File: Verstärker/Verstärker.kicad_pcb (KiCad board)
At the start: 2 copper layers, 59 parts, among them J3 ACJS-MHOM, J4 NRJ6HM-1, Q1 MJE13005G, Q1 MJE182G, Q12 MMBT5401, Q12 NPN, Q13 MMBT5401, Q13 NPN, Q2 MJE13005G, Q2 MJE172G, Q3 MMBT5551(RANGE:200-300), Q9 MMBT5551(RANGE:200-300)

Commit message: 29.04. Ende der VL
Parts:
- removed the Q1 at (207.0, 64.4)
- removed the Q1 at (237.5, 106.4)
- removed the Q12 at (77.0, 92.1)
- removed the Q12 at (237.5, 115.3)
- removed the Q13 at (52.0, 92.1)
- removed the Q13 at (237.5, 120.0)
- removed the Q2 at (163.0, 127.9)
- removed the Q2 at (237.5, 111.0)
- removed the TP3 at (209.5, 56.5)
- removed the TP3 at (157.8, 14.0)
- removed TP_GND1, TP_R2, TP_T2: OUT, TestPoint:TestPoint_Pad_D1.0mm
- removed TP_R1: IN, TestPoint:TestPoint_Pad_D1.0mm
- removed TP_S1: VCC -, TestPoint:TestPoint_Pad_D1.0mm
- added H1: OUT AMP B, MountingHole:MountingHole_2.2mm_M2_Pad_TopBottom, F.Cu at (167.8, 66.1)
- added H2: IN, MountingHole:MountingHole_2.2mm_M2_Pad_TopBottom, F.Cu at (53.0, 121.0)
- added H3: VCC +, MountingHole:MountingHole_2.2mm_M2_Pad_TopBottom, F.Cu at (167.8, 106.1)
- added H4: VCC -, MountingHole:MountingHole_2.2mm_M2_Pad_TopBottom, F.Cu at (153.8, 106.1)
- added H5: GND, MountingHole:MountingHole_2.2mm_M2_Pad_TopBottom, F.Cu at (37.5, 121.0)
- added H6: VCC GND, MountingHole:MountingHole_2.2mm_M2_Pad_TopBottom, F.Cu at (160.8, 106.1)
- added H7: GND, MountingHole:MountingHole_2.2mm_M2_Pad_TopBottom, F.Cu at (160.3, 66.1)
- added H8: OUT, MountingHole:MountingHole_2.2mm_M2_Pad_TopBottom, F.Cu at (152.8, 66.1)
- added H9: IN AMP B, MountingHole:MountingHole_2.2mm_M2_Pad_TopBottom, F.Cu at (45.5, 121.0)
- added Q1: MJE182G, project-custom:TO229P780X300X1364-3, F.Cu at (144.9, 77.1)
- added Q12: MMBT5401, Package_TO_SOT_SMD:SOT-23, F.Cu at (94.9, 82.5)
- added Q13: MMBT5401, Package_TO_SOT_SMD:SOT-23, F.Cu at (81.0, 82.5)
- added Q2: MJE172G, project-custom:TO229P780X300X1364-3, F.Cu at (144.8, 99.1)
- added TP3: Q2, TestPoint:TestPoint_Pad_D2.0mm, F.Cu at (143.2, 127.4)
- TP1: value TestPoint -> Output
- TP12: value TestPoint -> GND
- TP2: value TestPoint -> Q1
- moved TP12 144.4 mm to (73.0, 121.0)
- moved TP11 142.6 mm to (80.5, 121.0)
- moved TP10 141.0 mm to (88.5, 121.0)
- moved TP7 126.2 mm to (134.0, 128.0)
- moved TP1 120.2 mm to (162.5, 126.0)
- moved TP5 101.7 mm to (72.0, 57.5)
- moved J4 99.1 mm to (160.3, 80.2)
- moved TP8 94.1 mm to (85.0, 58.0)
- moved R12 85.2 mm to (129.8, 88.2), turned to -90 degrees
- moved C2 84.3 mm to (129.8, 83.8), turned to 90 degrees
- moved TP9 83.5 mm to (95.0, 58.0)
- moved TP4 78.3 mm to (103.5, 58.0)
- moved R4 76.1 mm to (136.0, 89.5), turned to 90 degrees
- moved TP6 66.3 mm to (109.0, 54.0)
- moved C1 64.1 mm to (100.0, 92.0), turned to 90 degrees
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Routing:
- net GND: track 0.00 -> 64.4 mm
- net Net-(D9-K): track 0.00 -> 43.6 mm
- net Net-(D1-A): track 0.00 -> 26.7 mm
- net Net-(D10-A): track 0.00 -> 12.9 mm
- net Net-(Q1-E): track 0.00 -> 3.94 mm
- net Net-(Q2-E): track 0.00 -> 3.92 mm

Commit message: 29.04. 15 Uhr
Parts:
- moved R8 19.3 mm to (63.0, 102.8)
- moved R13 16.5 mm to (57.5, 104.2)
- moved C6 15.5 mm to (67.8, 103.5)
- moved C7 15.0 mm to (65.5, 98.0)
- moved C4 14.6 mm to (94.2, 89.2), turned to 180 degrees
- moved TP9 12.6 mm to (82.8, 60.8)
- moved R10 9.60 mm to (87.8, 84.8), turned to 0 degrees
- moved C1 6.75 mm to (99.8, 98.8)
- moved TP8 6.56 mm to (89.2, 63.0)
- moved R7 6.52 mm to (99.5, 92.0)
- moved R3 6.49 mm to (87.8, 79.5), turned to 180 degrees
- moved D2 4.30 mm to (87.8, 88.2), turned to 180 degrees
- moved D3 3.56 mm to (87.8, 94.0), turned to 0 degrees
- moved Q13 2.11 mm to (79.8, 84.2), turned to 90 degrees
- moved R9 0.51 mm to (74.2, 84.5)
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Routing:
- net Net-(D2-K): track 0.00 -> 32.5 mm
- net Net-(Q12-E): track 0.00 -> 23.8 mm, vias 0 -> 2
- net Net-(D2-A): track 0.00 -> 20.0 mm
- net Net-(D10-A): track 12.9 -> 26.8 mm
- net Net-(Q13-C): track 0.00 -> 7.05 mm
- net Net-(C1-Pad2): track 0.00 -> 3.74 mm

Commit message: 04.05. PCB komplett
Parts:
- moved TP1 44.6 mm to (135.8, 90.3)
- moved TP3 36.0 mm to (128.6, 94.5)
- moved TP7 33.9 mm to (115.7, 99.5)
- moved R4 33.6 mm to (105.1, 102.6), turned to 0 degrees
- moved TP11 32.7 mm to (109.7, 106.1)
- moved TP2 26.4 mm to (127.5, 80.3)
- moved R14 24.9 mm to (101.0, 94.6), turned to 0 degrees
- moved TP12 24.6 mm to (90.0, 103.2)
- moved TP10 22.0 mm to (96.9, 100.7)
- moved TP4 22.0 mm to (98.9, 79.5)
- moved TP5 21.8 mm to (74.9, 79.1)
- moved TP6 21.2 mm to (124.5, 68.5)
- moved H1 20.2 mm to (147.7, 66.3)
- moved H2 20.1 mm to (64.2, 104.3)
- moved H5 20.1 mm to (48.7, 104.3)
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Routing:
- net Net-(D10-A): track 26.8 -> 102.2 mm, vias 0 -> 2
- net Net-(D1-A): track 26.7 -> 84.9 mm
- net Net-(D9-K): track 43.6 -> 96.7 mm
- net Net-(D1-K): track 0.00 -> 52.7 mm, vias 0 -> 2
- net Net-(D4-A): track 0.00 -> 46.9 mm, vias 0 -> 2
- net Net-(Q13-C): track 7.05 -> 31.2 mm
- net Net-(H2-Pad1): track 0.00 -> 23.1 mm
- net GND: track 64.4 -> 45.1 mm
- net Net-(H1-Pad1): track 0.00 -> 16.8 mm
- net Net-(D2-A): track 20.0 -> 30.5 mm
- net Net-(H9-Pad1): track 0.00 -> 10.1 mm
- net Net-(C6-Pad2): track 0.00 -> 8.57 mm
- net Net-(Q3-B): track 0.00 -> 7.03 mm
- net Net-(Q1-E): track 3.94 -> 9.29 mm
- net Net-(Q12-E): track 23.8 -> 29.0 mm
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- added copper zone on B.Cu, net GND
- added copper zone on F.Cu, net GND

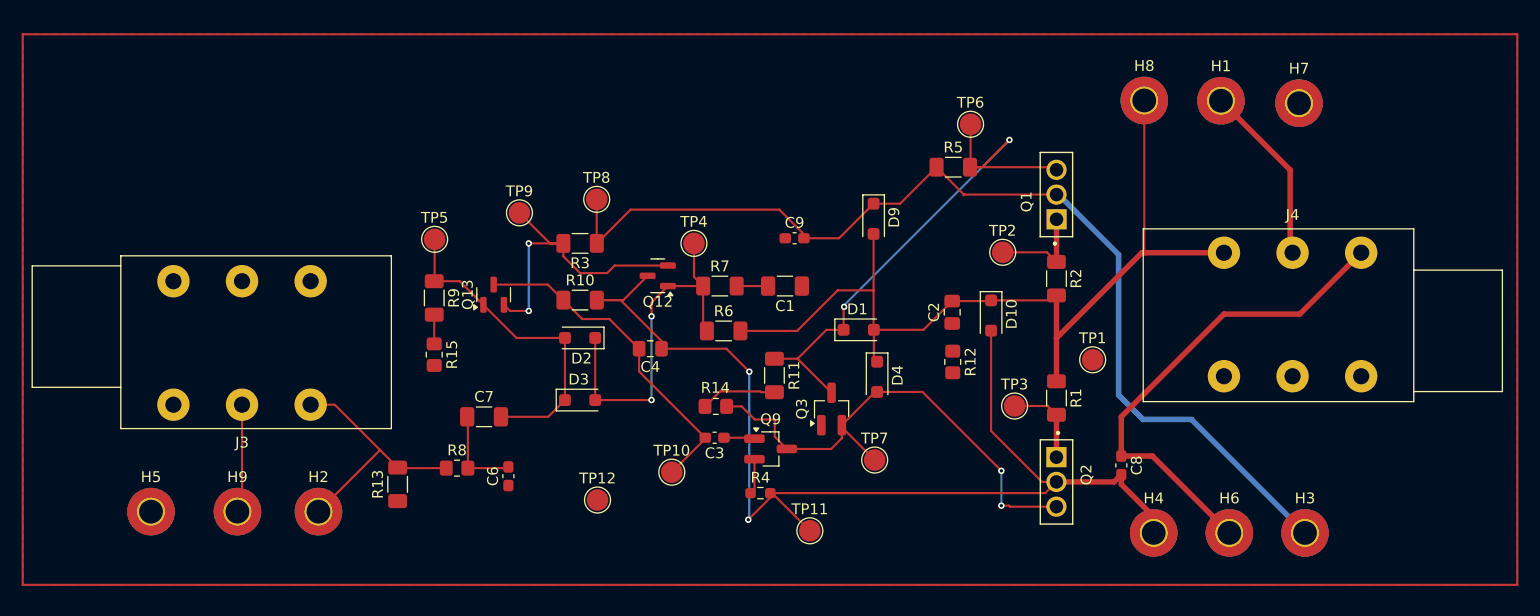
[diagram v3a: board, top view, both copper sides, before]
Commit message: dru Datei hinnzugefügt. Silcscreen der Testpoitns angepasst.
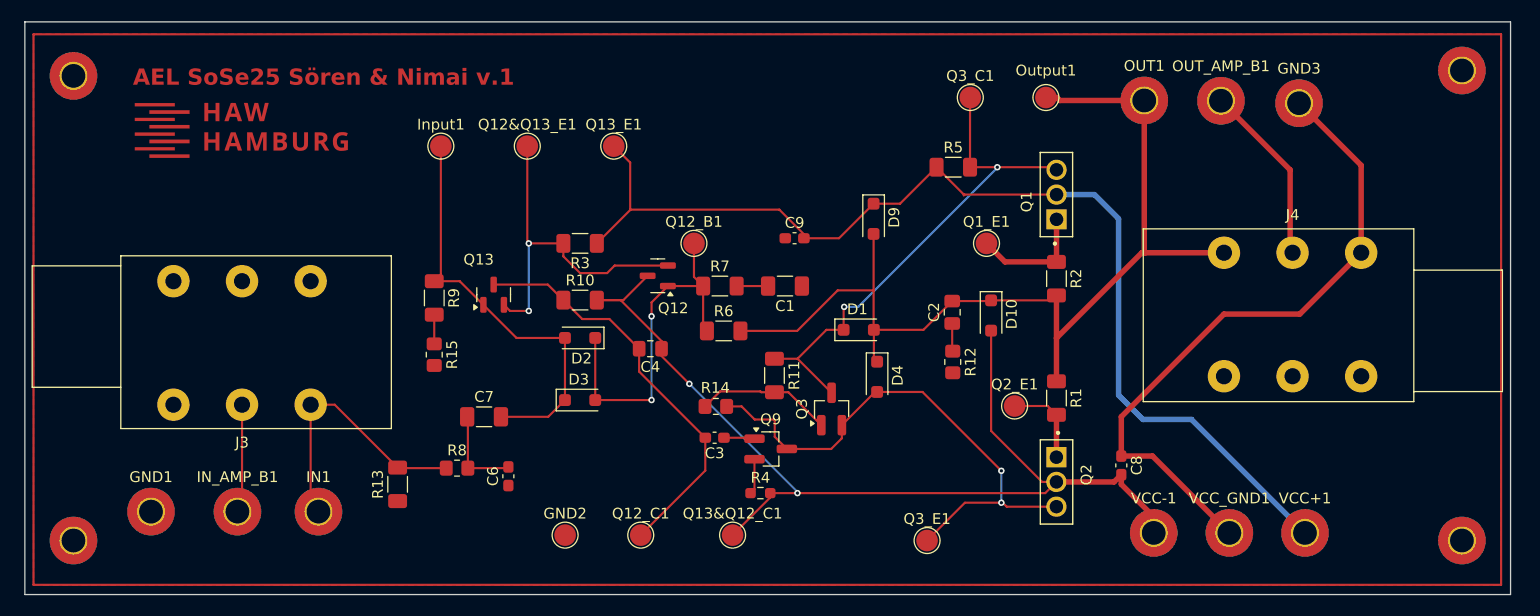
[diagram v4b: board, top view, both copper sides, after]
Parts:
- added G***: LOGO, LOGO, F.Cu at (57.0, 69.0)
- added GND4: H5, MountingHole:MountingHole_2.2mm_M2_Pad_TopBottom, F.Cu at (41.5, 64.0)
- added GND5: H5, MountingHole:MountingHole_2.2mm_M2_Pad_TopBottom, F.Cu at (41.5, 107.0)
- added GND6: H5, MountingHole:MountingHole_2.2mm_M2_Pad_TopBottom, F.Cu at (170.0, 63.5)
- added GND7: H5, MountingHole:MountingHole_2.2mm_M2_Pad_TopBottom, F.Cu at (170.0, 107.0)
- GND1: renamed from H5; value GND -> H5
- GND2: renamed from TP12; value GND -> TP12
- GND3: renamed from H7; value GND -> H7
- IN1: renamed from H2; value IN -> H2
- IN_AMP_B1: renamed from H9; value IN AMP B -> H9
- Input1: renamed from TP5; value Input -> TP5
- OUT1: renamed from H8; value OUT -> H8
- OUT_AMP_B1: renamed from H1; value OUT AMP B -> H1
- Output1: renamed from TP1; value Output -> TP1
- Q12&Q13_E1: renamed from TP9; value TestPoint -> TP9
- Q12_B1: renamed from TP4; value TestPoint -> TP4
- Q12_C1: renamed from TP10; value TestPoint -> TP10
- Q13&Q12_C1: renamed from TP11; value TestPoint -> TP11
- Q13_E1: renamed from TP8; value TestPoint -> TP8
- Q1_E1: renamed from TP2; value Q1 -> TP2
- Q2_E1: renamed from TP3; value Q2 -> TP3
- Q3_C1: renamed from TP6; value TestPoint -> TP6
- Q3_E1: renamed from TP7; value TestPoint -> TP7
- VCC+1: renamed from H3; value VCC + -> H3
- VCC-1: renamed from H4; value VCC - -> H4
- VCC_GND1: renamed from H6; value VCC GND -> H6
- moved Output1 24.7 mm to (131.5, 66.0)
- moved Q3_E1 8.89 mm to (120.5, 107.0)
- moved Input1 8.64 mm to (75.5, 70.5)
- moved Q13&Q12_C1 7.16 mm to (102.5, 106.5)
- moved Q12_C1 6.50 mm to (94.0, 106.5)
- moved Q12&Q13_E1 6.22 mm to (83.5, 70.5)
- moved Q13_E1 5.17 mm to (91.5, 70.5)
- moved GND2 4.42 mm to (87.0, 106.5)
- moved Q3_C1 2.48 mm to (124.5, 66.0)
- moved Q1_E1 1.71 mm to (126.0, 79.5)
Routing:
- net GND: track 45.1 -> 61.3 mm
- net Net-(D1-A): track 84.9 -> 94.1 mm
- net Net-(D2-A): track 30.5 -> 39.3 mm
- net Net-(D10-A): track 102.2 -> 95.1 mm
- net Net-(Q13-C): track 31.2 -> 38.2 mm
- net Net-(Q3-B): track 7.03 -> 12.6 mm
- net Net-(D9-K): track 96.7 -> 101.1 mm
- net Net-(D1-K): track 52.7 -> 48.4 mm
- net Net-(Q12-E): track 29.0 -> 32.8 mm
- net Net-(D4-A): track 46.9 -> 50.6 mm
- net Net-(C2-Pad1): track 0.00 -> 2.58 mm
- net Net-(IN1-Pad1): track 23.1 -> 25.2 mm
- net Net-(Q1-E): track 9.29 -> 11.1 mm
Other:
- board outline added: 137.5 x 53 mm
- board text added: "AEL SoSe25 Sören & Nimai v.1"

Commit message: Dings
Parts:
- moved GND2 0.50 mm to (87.0, 107.0)
- moved GND6 0.50 mm to (170.0, 64.0)
- moved Q12_C1 0.50 mm to (94.0, 107.0)
- moved Q13&Q12_C1 0.50 mm to (102.5, 107.0)
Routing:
- net Net-(D4-A): track 50.6 -> 53.8 mm, vias 2 -> 1
- net Net-(D1-A): track 94.1 -> 92.8 mm
- net Net-(D10-A): track 95.1 -> 95.8 mm, vias 2 -> 0
- net Net-(Q12-E): track 32.8 -> 32.7 mm, vias 2 -> 0
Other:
- board text added: "AEL SoSe25 Nimai & Sören v.1"
- board text removed: "AEL SoSe25 Sören & Nimai v.1"

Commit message: Weiter aufgeräumt
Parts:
- moved D2 1.75 mm to (88.4, 90.0)
- renumbered GND2 to GND, GND3 to GND, GND1 to GND, IN1 to IN, IN_AMP_B1 to IN_AMP_B, Input1 to Input, OUT1 to OUT, OUT_AMP_B1 to OUT_AMP_B, Output1 to Output, Q12&Q13_E1 to Q12&Q13_E, Q12_B1 to Q12_B, Q12_C1 to Q12_C, Q13&Q12_C1 to Q13&Q12_C, Q13_E1 to Q13_E, Q1_E1 to Q1_E, Q2_E1 to Q2_E, Q3_C1 to Q3_C, Q3_E1 to Q3_E, VCC+1 to VCC+, VCC-1 to VCC-, VCC_GND1 to VCC_GND
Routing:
- net Net-(D2-K): track 34.0 -> 32.2 mm
- net Net-(D2-A): track 39.3 -> 38.3 mm
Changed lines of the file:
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@@
 		(descr "SMD pad as test Point, diameter 2.0mm")
 		(tags "test point SMD pad")
-		(property "Reference" "GND2"
+		(property "Reference" "GND"
 			(at 0 -2.5 0)
 			(layer "F.SilkS")
@@
 		(at 132.48 77.2725 90)
 		(property "Reference" "Q1"
-			(at 1.625 -2.775 90)
+			(at 7.2725 0.02 180)
 			(layer "F.SilkS")
 			(effects
@@
 		(descr "SMD pad as test Point, diameter 2.0mm")
 		(tags "test point SMD pad")
-		(property "Reference" "Q12_C1"
+		(property "Reference" "Q12_C"
 			(at 0 -2.5 0)
 			(layer "F.SilkS")
@@
 		(tags "neutrik jack slim")
 		(property "Reference" "J4"
-			(at 6.35 -3.5 0)
+			(at 3.025 3.635 0)
 			(layer "F.SilkS")
 			(effects
@@
 		(tags "resistor handsolder")
 		(property "Reference" "R11"
-			(at 0 -1.83 90)
+			(at -3.225 -0.125 180)
 			(layer "F.SilkS")
 			(effects
@@
 			(at -0.127 -1.905 90)
 			(layer "F.SilkS")
+			(hide yes)
 			(effects
 				(font
@@
 		)
 		(fp_text user "${REFERENCE}"
-			(at -0.127 -1.905 90)
+			(at -0.175 -2.575 180)
 			(layer "F.Fab")
 			(effects
@@
 		(descr "Mounting Hole 2.2mm, M2")
 		(tags "mounting hole 2.2mm m2")
-		(property "Reference" "IN_AMP_B1"
+		(property "Reference" "IN_AMP_B"
 			(at 0 -3.2 0)
 			(layer "F.SilkS")
@@
 			(layer "F.CrtYd")
 		)
-		(fp_text user "${REFERENCE}"
-			(at 0 0 0)
-			(layer "F.Fab")
-			(effects
-				(font
-					(size 1 1)
-					(thickness 0.15)
-				)
-			)
-		)
 		(pad "1" thru_hole circle
 			(at 0 0)
@@
 		(descr "SMD pad as test Point, diameter 2.0mm")
 		(tags "test point SMD pad")
-		(property "Reference" "Input1"
+		(property "Reference" "Input"
 			(at 0 -1.998 0)
 			(layer "F.SilkS")
@@
 		(tags "SOT TO_SOT_SMD")
 		(property "Reference" "Q12"
-			(at -1.425 -3 0)
+			(at 0.075 2.5 0)
 			(layer "F.SilkS")
 			(effects
@@
 		(tags "capacitor handsolder")
 		(property "Reference" "C2"
-			(at 0 -1.68 90)
+			(at 2.875 -0.325 180)
 			(layer "F.SilkS")
 			(effects
@@
 		(tags "capacitor handsolder")
 		(property "Reference" "C1"
-			(at 0 -1.85 0)
+			(at 0 1.95 0)
 			(layer "F.SilkS")
 			(effects
@@
 		(tags "resistor handsolder")
 		(property "Reference" "R3"
-			(at 0 -1.83 0)
+			(at 0 2 0)
 			(layer "F.SilkS")
 			(effects
@@
 		(descr "Mounting Hole 2.2mm, M2")
 		(tags "mounting hole 2.2mm m2")
-		(property "Reference" "GND3"
+		(property "Reference" "GND"
 			(at 0 -3.2 0)
 			(layer "F.SilkS")
@@
 		(tags "resistor handsolder")
 		(property "Reference" "R1"
-			(at 0 -1.83 90)
+			(at -3.315 -1.83 180)
 			(layer "F.SilkS")
 			(effects
@@
 		(tags "resistor handsolder")
 		(property "Reference" "R15"
-			(at 0 -1.65 90)
+			(at 1.2 -2.6125 180)
 			(layer "F.SilkS")
 			(effects
@@
 		(descr "SMD pad as test Point, diameter 2.0mm")
 		(tags "test point SMD pad")
-		(property "Reference" "Q1_E1"
+		(property "Reference" "Q1_E"
 			(at 0 -1.998 0)
 			(layer "F.SilkS")
@@
 		(descr "Mounting Hole 2.2mm, M2")
 		(tags "mounting hole 2.2mm m2")
-		(property "Reference" "OUT_AMP_B1"
+		(property "Reference" "OUT_AMP_B"
 			(at 0 -3.2 0)
 			(layer "F.SilkS")
@@
 			(layer "F.CrtYd")
 		)
-		(fp_text user "${REFERENCE}"
-			(at 0 0 0)
-			(layer "F.Fab")
-			(effects
-				(font
-					(size 1 1)
-					(thickness 0.15)
-				)
-			)
-		)
 		(pad "1" thru_hole circle
 			(at 0 0)
@@
 		(descr "Mounting Hole 2.2mm, M2")
 		(tags "mounting hole 2.2mm m2")
-		(property "Reference" "VCC_GND1"
+		(property "Reference" "VCC_GND"
 			(at 0 -3.2 0)
 			(layer "F.SilkS")
@@
 		(descr "SMD pad as test Point, diameter 2.0mm")
 		(tags "test point SMD pad")
-		(property "Reference" "Q12&Q13_E1"
+		(property "Reference" "Q12&Q13_E"
 			(at 0 -1.998 0)
 			(layer "F.SilkS")
@@
 		(descr "SMD pad as test Point, diameter 2.0mm")
 		(tags "test point SMD pad")
-		(property "Reference" "Q2_E1"
+		(property "Reference" "Q2_E"
 			(at -0.1 -2.55 0)
 			(layer "F.SilkS")
@@
 		(at 132.47 99.2875 -90)
 		(property "Reference" "Q2"
-			(at 1.625 -2.775 90)
+			(at 7.2125 -0.03 180)
 			(layer "F.SilkS")
 			(effects
@@
 		(descr "Mounting Hole 2.2mm, M2")
 		(tags "mounting hole 2.2mm m2")
-		(property "Reference" "VCC-1"
+		(property "Reference" "VCC-"
 			(at 0 -3.2 0)
 			(layer "F.SilkS")
@@
 		(descr "Mounting Hole 2.2mm, M2")
 		(tags "mounting hole 2.2mm m2")
-		(property "Reference" "VCC+1"
+		(property "Reference" "VCC+"
 			(at 0 -3.2 0)
 			(layer "F.SilkS")
@@
 		(tags "resistor handsolder")
 		(property "Reference" "R12"
-			(at 0 -1.65 90)
+			(at -0.475 2.875 180)
 			(layer "F.SilkS")
 			(effects
@@
 		(tags "capacitor handsolder")
 		(property "Reference" "C6"
-			(at 0 -1.43 90)
+			(at 2.55 0.25 180)
 			(layer "F.SilkS")
 			(effects
@@
 		(tags "capacitor handsolder")
 		(property "Reference" "C8"
-			(at 0 -1.43 90)
+			(at -1.045 -2.025 180)
 			(layer "F.SilkS")
 			(effects
@@
 		(tags "SOT-23")
 		(property "Reference" "Q3"
-			(at 0 -2.75 90)
+			(at 3.325 -0.1625 180)
 			(layer "F.SilkS")
 			(effects
@@
 		(descr "SMD pad as test Point, diameter 2.0mm")
 		(tags "test point SMD pad")
-		(property "Reference" "Q13_E1"
+		(property "Reference" "Q13_E"
 			(at 0 -1.998 0)
 			(layer "F.SilkS")
@@
 		(descr "SMD pad as test Point, diameter 2.0mm")
 		(tags "test point SMD pad")
-		(property "Reference" "Q3_C1"
+		(property "Reference" "Q3_C"
 			(at 0 -1.998 0)
 			(layer "F.SilkS")
@@
 		(tags "capacitor handsolder")
 		(property "Reference" "C3"
-			(at 0 -1.43 0)
+			(at 0 -1.5125 0)
 			(layer "F.SilkS")
 			(effects
@@
 		(descr "SMD pad as test Point, diameter 2.0mm")
 		(tags "test point SMD pad")
-		(property "Reference" "Q12_B1"
+		(property "Reference" "Q12_B"
 			(at 0 -1.998 0)
 			(layer "F.SilkS")
@@
 	(footprint "Diode_SMD:D_SOD-123F"
 		(layer "F.Cu")
-		(at 88.3875 88.25 180)
+		(at 88.3875 90 180)
 		(descr "D_SOD-123F")
 		(tags "D_SOD-123F")
 		(property "Reference" "D2"
-			(at -0.127 -1.905 0)
+			(at -0.1125 2 0)
 			(layer "F.SilkS")
 			(effects
@@
 		)
 		(fp_text user "${REFERENCE}"
-			(at -0.127 -1.905 0)
+			(at -0.1125 2 0)
 			(layer "F.Fab")
 			(effects
@@
 		(descr "SMD pad as test Point, diameter 2.0mm")
 		(tags "test point SMD pad")
-		(property "Reference" "Q13&Q12_C1"
+		(property "Reference" "Q13&Q12_C"
 			(at 0 -2.5 0)
 			(layer "F.SilkS")
@@
 		(descr "Mounting Hole 2.2mm, M2")
 		(tags "mounting hole 2.2mm m2")
-		(property "Reference" "GND1"
+		(property "Reference" "GND"
 			(at 0 -3.2 0)
 			(layer "F.SilkS")
@@
 		(tags "resistor handsolder")
 		(property "Reference" "R9"
-			(at 0 -1.83 90)
+			(at 1.95 -2.1125 180)
 			(layer "F.SilkS")
 			(effects
@@
 		(descr "Mounting Hole 2.2mm, M2")
 		(tags "mounting hole 2.2mm m2")
-		(property "Reference" "OUT1"
+		(property "Reference" "OUT"
 			(at 0 -3.2 0)
 			(layer "F.SilkS")
@@
 		(descr "Mounting Hole 2.2mm, M2")
 		(tags "mounting hole 2.2mm m2")
-		(property "Reference" "IN1"
+		(property "Reference" "IN"
 			(at 0 -3.2 0)
 			(layer "F.SilkS")
@@
 		(tags "resistor handsolder")
 		(property "Reference" "R2"
-			(at 0 -1.83 90)
+			(at -2.265 -2.025 180)
 			(layer "F.SilkS")
 			(effects
@@
 		(descr "SMD pad as test Point, diameter 2.0mm")
 		(tags "test point SMD pad")
-		(property "Reference" "Q3_E1"
+		(property "Reference" "Q3_E"
 			(at 0 -2.5 0)
 			(layer "F.SilkS")
@@
 		(tags "resistor handsolder")
 		(property "Reference" "R13"
-			(at 0 -1.83 90)
+			(at 3.3 0.5 180)
 			(layer "F.SilkS")
 			(effects
@@
 		(descr "SMD pad as test Point, diameter 2.0mm")
 		(tags "test point SMD pad")
-		(property "Reference" "Output1"
+		(property "Reference" "Output"
 			(at 0 -2.5 0)
 			(layer "F.SilkS")
@@
 		(tags "D_SOD-123F")
 		(property "Reference" "D4"
-			(at -0.127 -1.905 90)
+			(at -0.85 -2.125 180)
 			(layer "F.SilkS")
+			(hide yes)
 			(effects
 				(font
@@
 		)
 		(fp_text user "${REFERENCE}"
-			(at -0.127 -1.905 90)
+			(at 0.15 -2.125 180)
 			(layer "F.Fab")
 			(effects
@@
 	)
 	(segment
-		(start 79.4375 85.1875)
-		(end 82.5 88.25)
+		(start 84.25 90)
+		(end 86.9875 90)
 		(width 0.2)
 		(layer "F.Cu")
@@
 	)
 	(segment
-		(start 85.4375 95.55)
-		(end 86.9875 94)
+		(start 79.4375 85.1875)
+		(end 84.25 90)
 		(width 0.2)
 		(layer "F.Cu")
@@
 	)
 	(segment
-		(start 82.5 88.25)
-		(end 86.9875 88.25)
+		(start 85.4375 95.55)
+		(end 86.9875 94)
 		(width 0.2)
 		(layer "F.Cu")
@@
 	)
 	(segment
-		(start 77.25 83)
-		(end 79.4375 85.1875)
+		(start 86.9875 90)
+		(end 86.9875 94)
 		(width 0.2)
 		(layer "F.Cu")
@@
 	)
 	(segment
-		(start 86.9875 88.25)
-		(end 86.9875 94)
+		(start 77.25 83)
+		(end 79.4375 85.1875)
 		(width 0.2)
 		(layer "F.Cu")
@@
 	)
 	(segment
+		(start 89.7875 90)
+		(end 89.7875 94)
+		(width 0.2)
+		(layer "F.Cu")
+		(net 12)
+	)
+	(segment
 		(start 95 86.25)
 		(end 95 84.9625)
@@
 		(width 0.2)
 		(layer "F.Cu")
-		(net 12)
-	)
-	(segment
-		(start 89.7875 88.25)
-		(end 89.7875 94)
-		(width 0.2)
-		(layer "F.Cu")
